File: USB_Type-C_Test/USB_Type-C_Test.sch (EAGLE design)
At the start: 51 parts, among them J1 105450-0101, U1 P8X32A-Q44, U2 FT230XQ-R, U4 CAT24C512WI-GT3, U6 NCP1117LPST33T3G, U7 IRLML6401TRPBF, X1 ABMM-6.000MHZ-B2-T

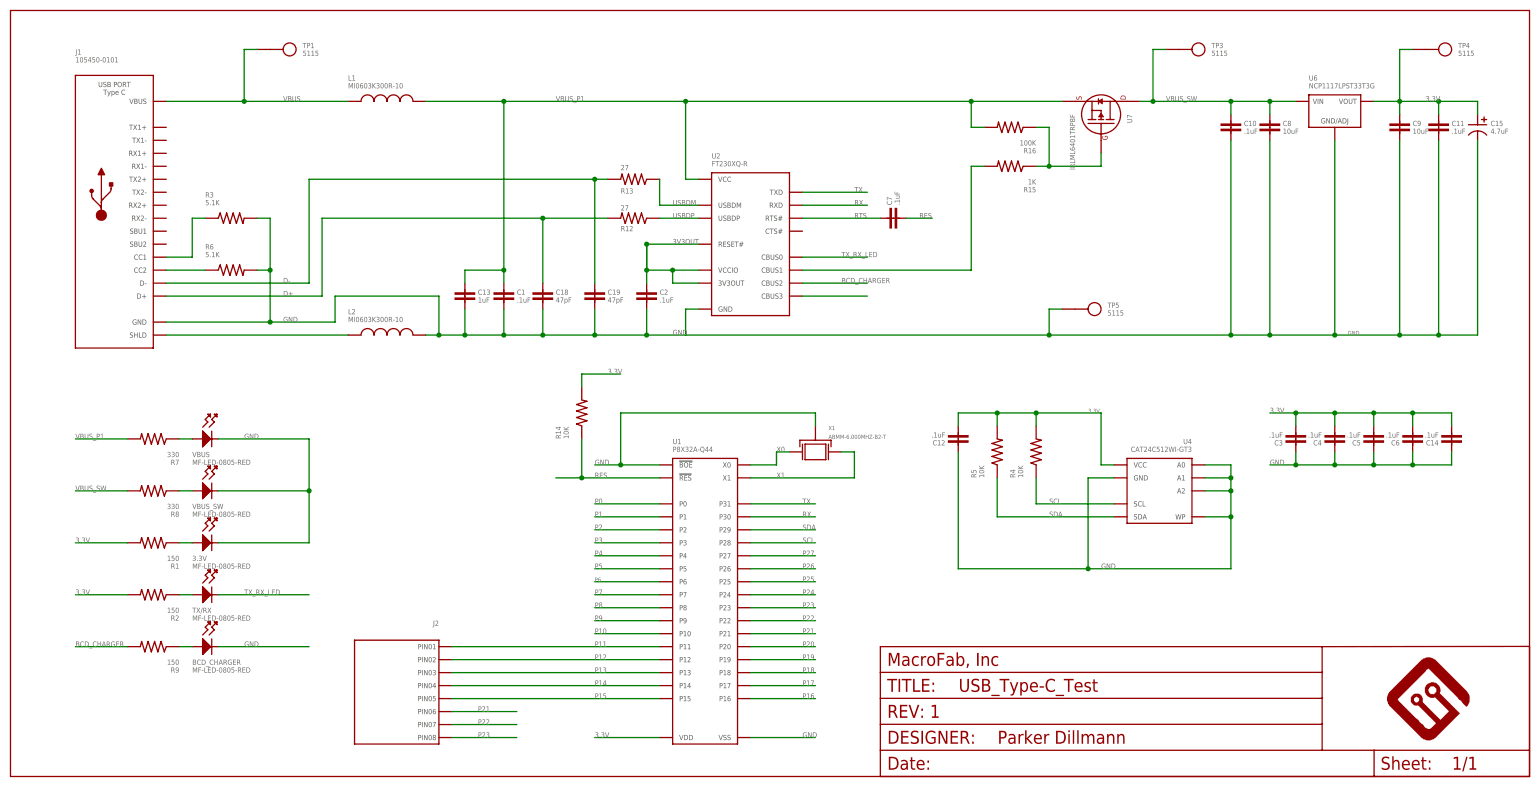
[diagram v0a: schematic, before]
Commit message: Fixing the Type C connector.
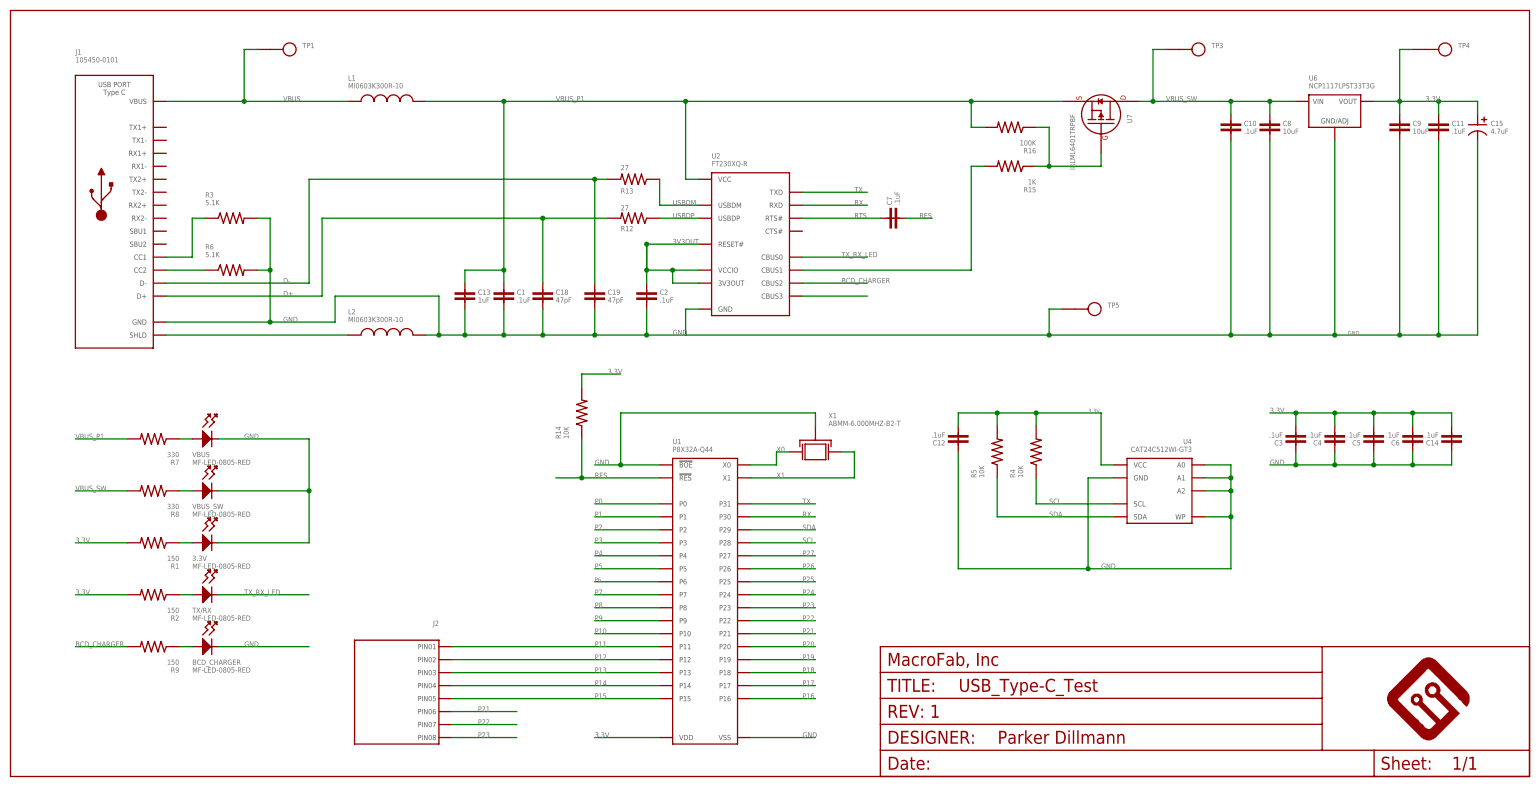
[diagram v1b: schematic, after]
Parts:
- J1: MPN (none) -> 105450-0101
- TP1, TP3, TP4, TP5: value 5115 -> (none)
- X1: device MF_Frequency_Control:XTL_7MMX5MM -> MF_Frequency_Control:CYRSTAL_GND_ABMM

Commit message: Finishing up the board design.
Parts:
- removed R6: 5.1K, PP_Passives:RESISTOR_0603
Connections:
- removed net N$5: J1.CC2, R6.1
- net GND: no longer R6.2
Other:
- moved on the sheet: R3
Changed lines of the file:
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@@
 <grid distance="0.1" unitdist="inch" unit="inch" style="lines" multiple="1" display="no" altdistance="0.01" altunitdist="inch" altunit="inch"/>
 <layers>
-<layer number="1" name="Top" color="4" fill="1" visible="yes" active="no"/>
-<layer number="2" name="Route2" color="1" fill="3" visible="yes" active="no"/>
-<layer number="3" name="Route3" color="4" fill="3" visible="yes" active="no"/>
-<layer number="4" name="Route4" color="1" fill="4" visible="yes" active="no"/>
-<layer number="5" name="Route5" color="4" fill="4" visible="yes" active="no"/>
-<layer number="6" name="Route6" color="1" fill="8" visible="yes" active="no"/>
-<layer number="7" name="Route7" color="4" fill="8" visible="yes" active="no"/>
-<layer number="8" name="Route8" color="1" fill="2" visible="yes" active="no"/>
-<layer number="9" name="Route9" color="4" fill="2" visible="yes" active="no"/>
-<layer number="10" name="Route10" color="1" fill="7" visible="yes" active="no"/>
-<layer number="11" name="Route11" color="4" fill="7" visible="yes" active="no"/>
-<layer number="12" name="Route12" color="1" fill="5" visible="yes" active="no"/>
-<layer number="13" name="Route13" color="4" fill="5" visible="yes" active="no"/>
-<layer number="14" name="Route14" color="1" fill="6" visible="yes" active="no"/>
-<layer number="15" name="Route15" color="4" fill="6" visible="yes" active="no"/>
-<layer number="16" name="Bottom" color="1" fill="1" visible="yes" active="no"/>
-<layer number="17" name="Pads" color="2" fill="1" visible="yes" active="no"/>
-<layer number="18" name="Vias" color="2" fill="1" visible="yes" active="no"/>
-<layer number="19" name="Unrouted" color="6" fill="1" visible="yes" active="no"/>
-<layer number="20" name="Dimension" color="15" fill="1" visible="yes" active="no"/>
-<layer number="21" name="tPlace" color="7" fill="1" visible="yes" active="no"/>
-<layer number="22" name="bPlace" color="7" fill="1" visible="yes" active="no"/>
-<layer number="23" name="tOrigins" color="15" fill="1" visible="yes" active="no"/>
-<layer number="24" name="bOrigins" color="15" fill="1" visible="yes" active="no"/>
-<layer number="25" name="tNames" color="7" fill="1" visible="yes" active="no"/>
-<layer number="26" name="bNames" color="7" fill="1" visible="yes" active="no"/>
-<layer number="27" name="tValues" color="7" fill="1" visible="yes" active="no"/>
-<layer number="28" name="bValues" color="7" fill="1" visible="yes" active="no"/>
+<layer number="1" name="Top" color="4" fill="1" visible="no" active="no"/>
+<layer number="2" name="Route2" color="1" fill="3" visible="no" active="no"/>
+<layer number="3" name="Route3" color="4" fill="3" visible="no" active="no"/>
+<layer number="4" name="Route4" color="1" fill="4" visible="no" active="no"/>
+<layer number="5" name="Route5" color="4" fill="4" visible="no" active="no"/>
+<layer number="6" name="Route6" color="1" fill="8" visible="no" active="no"/>
+<layer number="7" name="Route7" color="4" fill="8" visible="no" active="no"/>
+<layer number="8" name="Route8" color="1" fill="2" visible="no" active="no"/>
+<layer number="9" name="Route9" color="4" fill="2" visible="no" active="no"/>
+<layer number="10" name="Route10" color="1" fill="7" visible="no" active="no"/>
+<layer number="11" name="Route11" color="4" fill="7" visible="no" active="no"/>
+<layer number="12" name="Route12" color="1" fill="5" visible="no" active="no"/>
+<layer number="13" name="Route13" color="4" fill="5" visible="no" active="no"/>
+<layer number="14" name="Route14" color="1" fill="6" visible="no" active="no"/>
+<layer number="15" name="Route15" color="4" fill="6" visible="no" active="no"/>
+<layer number="16" name="Bottom" color="1" fill="1" visible="no" active="no"/>
+<layer number="17" name="Pads" color="2" fill="1" visible="no" active="no"/>
+<layer number="18" name="Vias" color="2" fill="1" visible="no" active="no"/>
+<layer number="19" name="Unrouted" color="6" fill="1" visible="no" active="no"/>
+<layer number="20" name="Dimension" color="15" fill="1" visible="no" active="no"/>
+<layer number="21" name="tPlace" color="7" fill="1" visible="no" active="no"/>
+<layer number="22" name="bPlace" color="7" fill="1" visible="no" active="no"/>
+<layer number="23" name="tOrigins" color="15" fill="1" visible="no" active="no"/>
+<layer number="24" name="bOrigins" color="15" fill="1" visible="no" active="no"/>
+<layer number="25" name="tNames" color="7" fill="1" visible="no" active="no"/>
+<layer number="26" name="bNames" color="7" fill="1" visible="no" active="no"/>
+<layer number="27" name="tValues" color="7" fill="1" visible="no" active="no"/>
+<layer number="28" name="bValues" color="7" fill="1" visible="no" active="no"/>
 <layer number="29" name="tStop" color="7" fill="3" visible="no" active="no"/>
 <layer number="30" name="bStop" color="7" fill="6" visible="no" active="no"/>
@@
 <layer number="35" name="tGlue" color="7" fill="4" visible="no" active="no"/>
 <layer number="36" name="bGlue" color="7" fill="5" visible="no" active="no"/>
-<layer number="37" name="tTest" color="7" fill="1" visible="yes" active="no"/>
-<layer number="38" name="bTest" color="7" fill="1" visible="yes" active="no"/>
+<layer number="37" name="tTest" color="7" fill="1" visible="no" active="no"/>
+<layer number="38" name="bTest" color="7" fill="1" visible="no" active="no"/>
 <layer number="39" name="tKeepout" color="4" fill="11" visible="no" active="no"/>
 <layer number="40" name="bKeepout" color="1" fill="11" visible="no" active="no"/>
@@
 <layer number="44" name="Drills" color="7" fill="1" visible="no" active="no"/>
 <layer number="45" name="Holes" color="7" fill="1" visible="no" active="no"/>
-<layer number="46" name="Milling" color="3" fill="1" visible="yes" active="no"/>
-<layer number="47" name="Measures" color="7" fill="1" visible="yes" active="no"/>
-<layer number="48" name="Document" color="7" fill="1" visible="yes" active="no"/>
-<layer number="49" name="Reference" color="7" fill="1" visible="yes" active="no"/>
-<layer number="50" name="dxf" color="7" fill="1" visible="yes" active="no"/>
-<layer number="51" name="tDocu" color="7" fill="1" visible="yes" active="no"/>
-<layer number="52" name="bDocu" color="7" fill="1" visible="yes" active="no"/>
-<layer number="53" name="tGND_GNDA" color="7" fill="9" visible="yes" active="no"/>
-<layer number="54" name="bGND_GNDA" color="1" fill="9" visible="yes" active="no"/>
-<layer number="56" name="wert" color="7" fill="1" visible="yes" active="no"/>
+<layer number="46" name="Milling" color="3" fill="1" visible="no" active="no"/>
+<layer number="47" name="Measures" color="7" fill="1" visible="no" active="no"/>
+<layer number="48" name="Document" color="7" fill="1" visible="no" active="no"/>
+<layer number="49" name="Reference" color="7" fill="1" visible="no" active="no"/>
+<layer number="50" name="dxf" color="7" fill="1" visible="no" active="no"/>
+<layer number="51" name="tDocu" color="7" fill="1" visible="no" active="no"/>
+<layer number="52" name="bDocu" color="7" fill="1" visible="no" active="no"/>
+<layer number="53" name="tGND_GNDA" color="7" fill="9" visible="no" active="no"/>
+<layer number="54" name="bGND_GNDA" color="1" fill="9" visible="no" active="no"/>
+<layer number="56" name="wert" color="7" fill="1" visible="no" active="no"/>
 <layer number="90" name="Modules" color="5" fill="1" visible="yes" active="yes"/>
 <layer number="91" name="Nets" color="2" fill="1" visible="yes" active="yes"/>
@@
 <part name="C19" library="PP_Passives" deviceset="CAPACITOR_NON_POLAR" device="_0603" value="47pF"/>
 <part name="R3" library="PP_Passives" deviceset="RESISTOR" device="_0603" value="5.1K"/>
-<part name="R6" library="PP_Passives" deviceset="RESISTOR" device="_0603" value="5.1K"/>
 <part name="TP1" library="PP_Connectors" deviceset="TEST_POINT_SINGLE" device="_KEYSTONE_5115-5119"/>
 <part name="TP3" library="PP_Connectors" deviceset="TEST_POINT_SINGLE" device="_KEYSTONE_5115-5119"/>
@@
 <instance part="C18" gate="G$1" x="-66.04" y="68.58"/>
 <instance part="C19" gate="G$1" x="-55.88" y="68.58"/>
-<instance part="R3" gate="G$1" x="-127" y="83.82"/>
-<instance part="R6" gate="G$1" x="-127" y="73.66"/>
+<instance part="R3" gate="G$1" x="-127" y="76.2"/>
 <instance part="TP1" gate="G$1" x="-119.38" y="116.84"/>
 <instance part="TP3" gate="G$1" x="58.42" y="116.84"/>
@@
 <pinref part="R3" gate="G$1" pin="2"/>
 <wire x1="-119.38" y1="63.5" x2="-139.7" y2="63.5" width="0.1524" layer="91"/>
-<wire x1="-121.92" y1="83.82" x2="-119.38" y2="83.82" width="0.1524" layer="91"/>
-<wire x1="-119.38" y1="83.82" x2="-119.38" y2="73.66" width="0.1524" layer="91"/>
-<pinref part="R6" gate="G$1" pin="2"/>
-<wire x1="-119.38" y1="73.66" x2="-121.92" y2="73.66" width="0.1524" layer="91"/>
-<wire x1="-119.38" y1="73.66" x2="-119.38" y2="63.5" width="0.1524" layer="91"/>
+<wire x1="-121.92" y1="76.2" x2="-119.38" y2="76.2" width="0.1524" layer="91"/>
+<wire x1="-119.38" y1="76.2" x2="-119.38" y2="63.5" width="0.1524" layer="91"/>
 <junction x="-119.38" y="63.5"/>
-<junction x="-119.38" y="73.66"/>
 <wire x1="88.9" y1="60.96" x2="101.6" y2="60.96" width="0.1524" layer="91"/>
 <wire x1="101.6" y1="60.96" x2="109.22" y2="60.96" width="0.1524" layer="91"/>
@@
 </segment>
 </net>
-<net name="N$5" class="0">
-<segment>
-<pinref part="J1" gate="G$1" pin="CC2"/>
-<pinref part="R6" gate="G$1" pin="1"/>
-<wire x1="-139.7" y1="73.66" x2="-132.08" y2="73.66" width="0.1524" layer="91"/>
-</segment>
-</net>
 <net name="N$6" class="0">
 <segment>
 <pinref part="J1" gate="G$1" pin="CC1"/>
-<wire x1="-139.7" y1="76.2" x2="-134.62" y2="76.2" width="0.1524" layer="91"/>
-<wire x1="-134.62" y1="76.2" x2="-134.62" y2="83.82" width="0.1524" layer="91"/>
+<wire x1="-139.7" y1="76.2" x2="-132.08" y2="76.2" width="0.1524" layer="91"/>
 <pinref part="R3" gate="G$1" pin="1"/>
-<wire x1="-134.62" y1="83.82" x2="-132.08" y2="83.82" width="0.1524" layer="91"/>
-</segment>
-</net>
+</segment>
+</net>
